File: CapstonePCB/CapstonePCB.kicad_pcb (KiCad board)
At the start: 2 copper layers, 4 parts, among them J1 Conn_02x40_Counter_Clockwise, J2 Barrel_Jack, U1 NUCLEO64-F411RE, U2 LP-MSPM0G3507

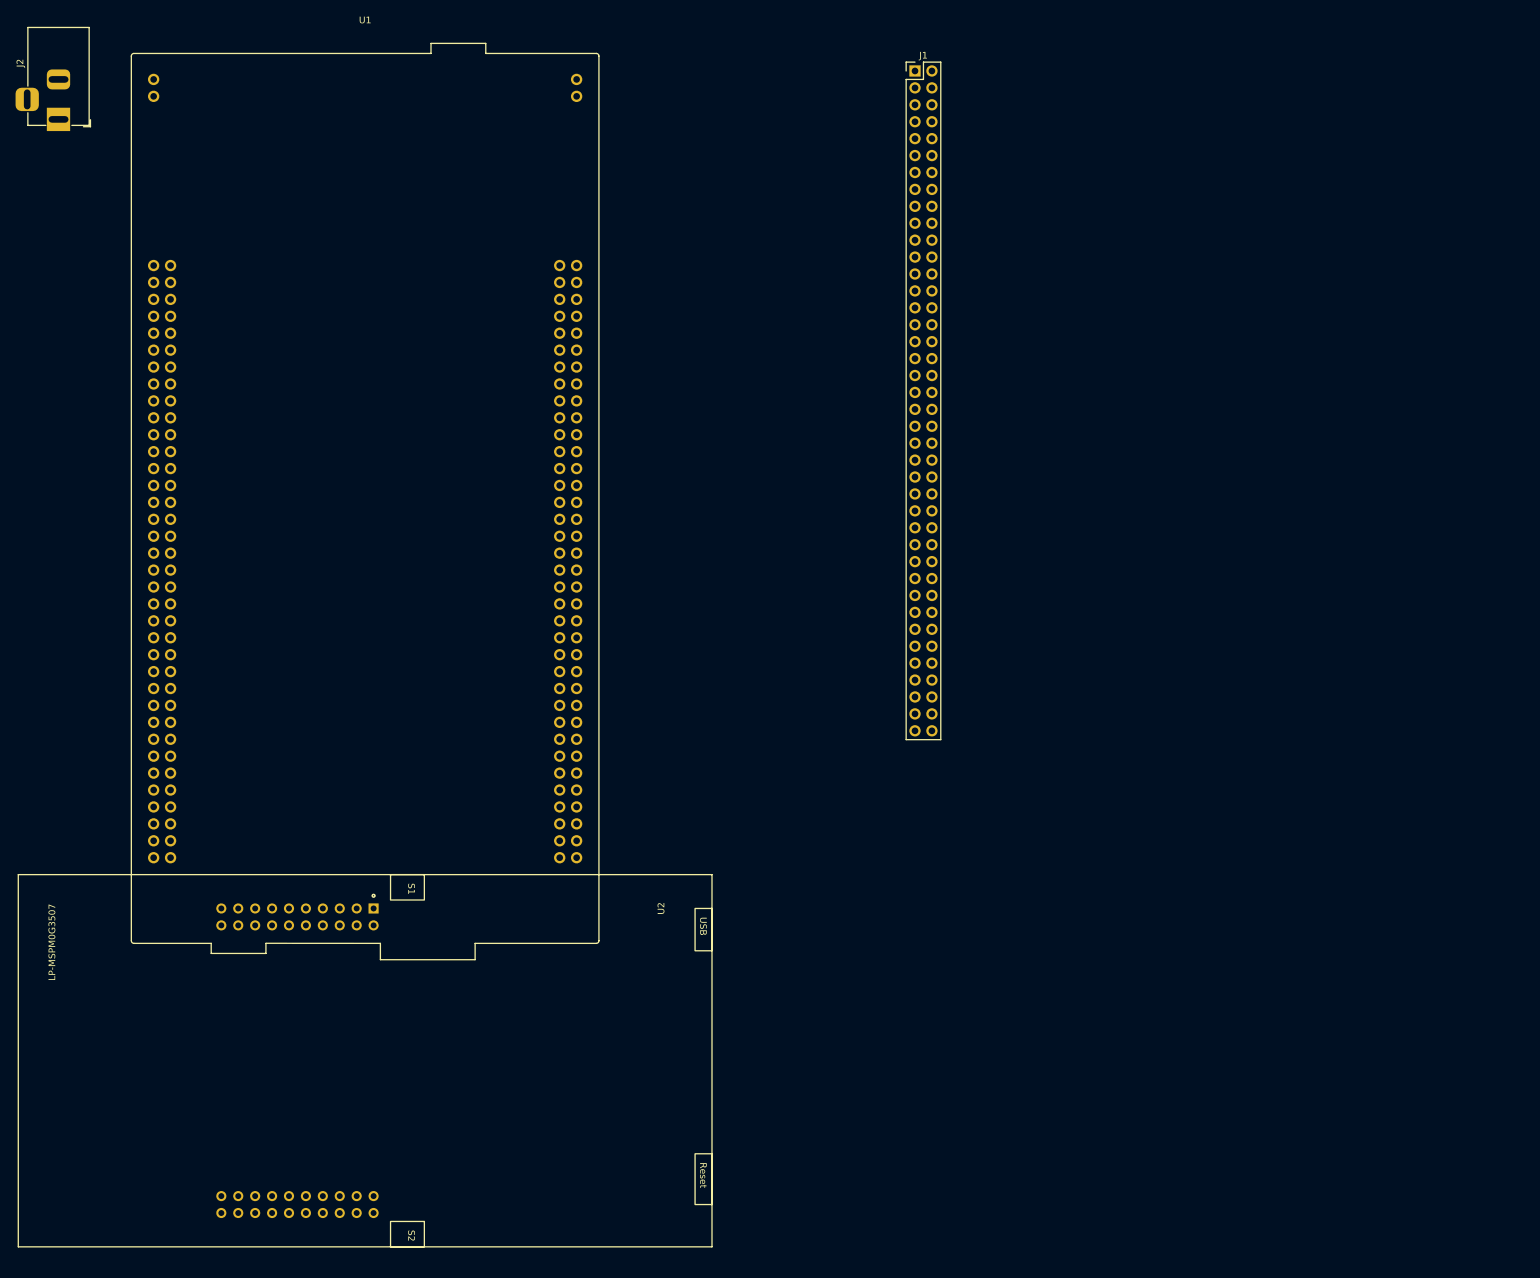
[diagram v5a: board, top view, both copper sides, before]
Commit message: Routed connections for header pins
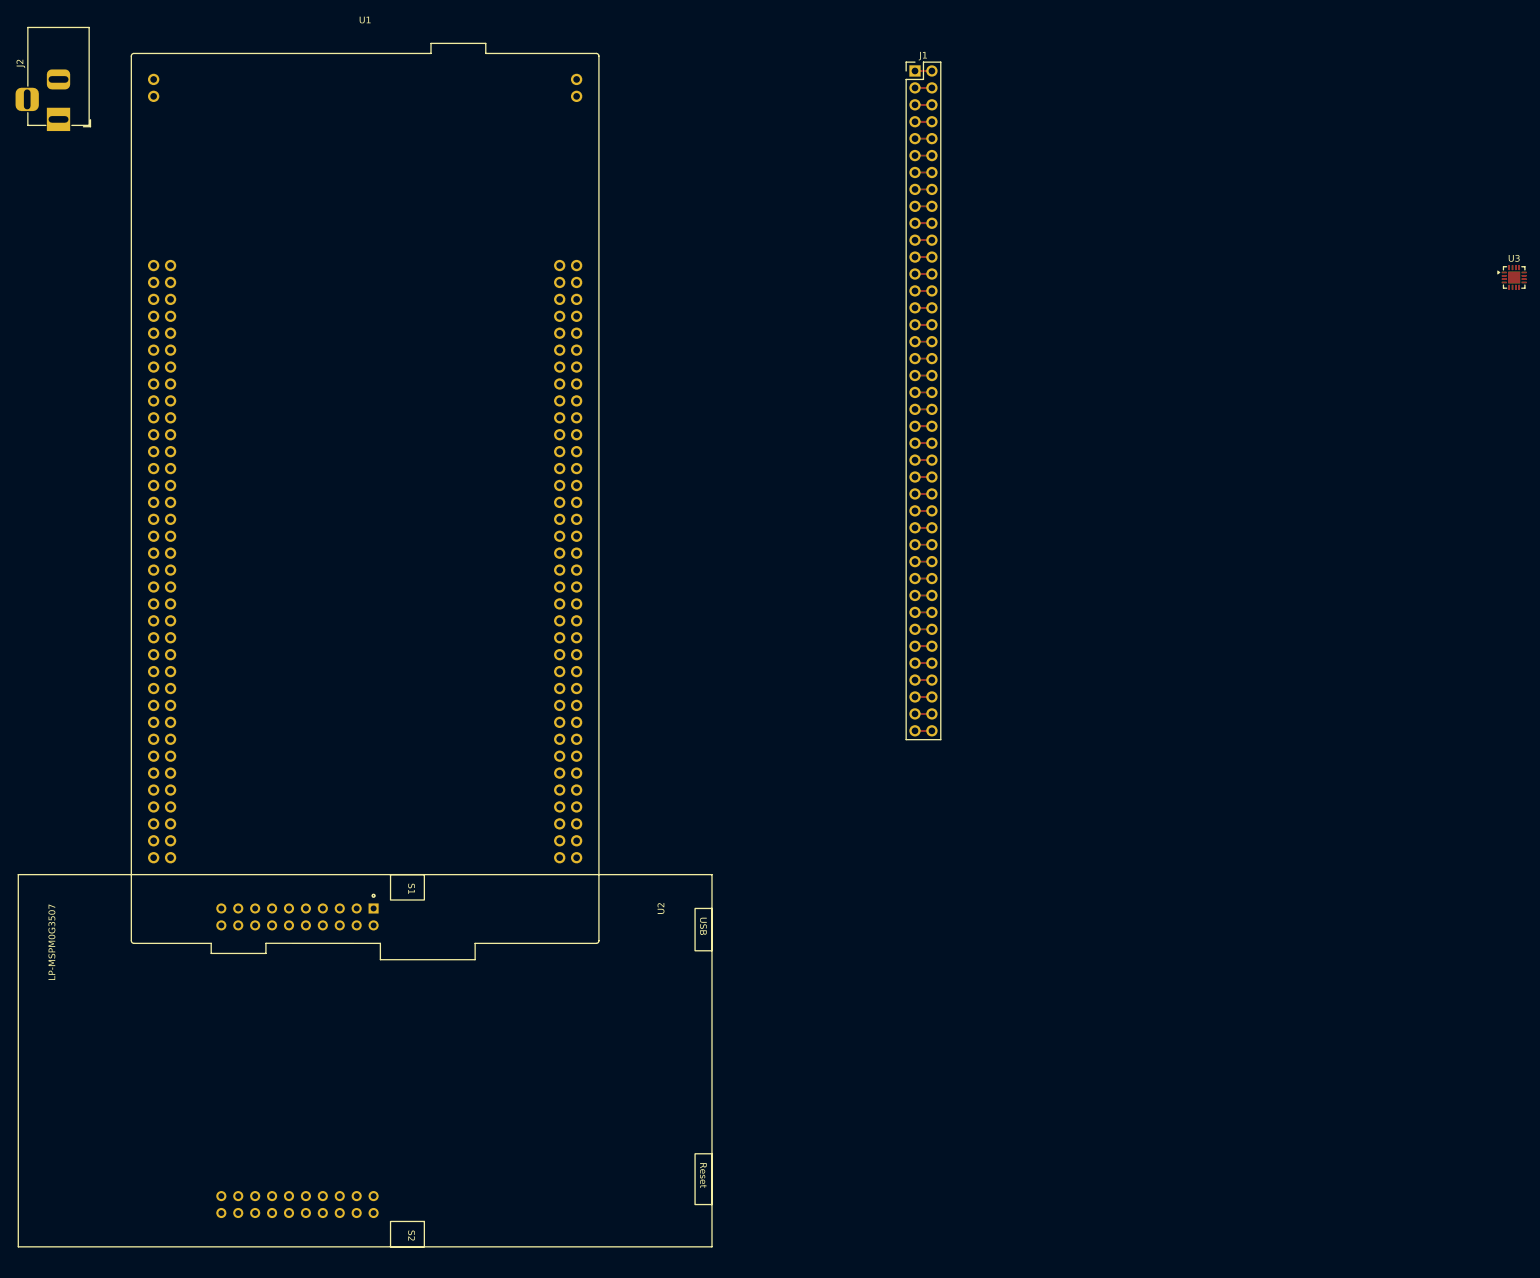
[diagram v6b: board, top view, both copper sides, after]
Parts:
- added U3: STSPIN220, Package_DFN_QFN:VQFN-16-1EP_3x3mm_P0.5mm_EP1.8x1.8mm, F.Cu at (237.3, 47.5)
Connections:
- J1 pad 10: unconnected-(J1-Pin_10-Pad10) -> Net-(J1-Pin_10)
- J1 pad 11: unconnected-(J1-Pin_11-Pad11) -> Net-(J1-Pin_11)
- J1 pad 12: unconnected-(J1-Pin_12-Pad12) -> Net-(J1-Pin_11)
- J1 pad 13: unconnected-(J1-Pin_13-Pad13) -> Net-(J1-Pin_13)
- J1 pad 14: unconnected-(J1-Pin_14-Pad14) -> Net-(J1-Pin_13)
- J1 pad 15: unconnected-(J1-Pin_15-Pad15) -> Net-(J1-Pin_15)
- J1 pad 16: unconnected-(J1-Pin_16-Pad16) -> Net-(J1-Pin_15)
- J1 pad 17: unconnected-(J1-Pin_17-Pad17) -> Net-(J1-Pin_17)
- J1 pad 18: unconnected-(J1-Pin_18-Pad18) -> Net-(J1-Pin_17)
- J1 pad 19: unconnected-(J1-Pin_19-Pad19) -> Net-(J1-Pin_19)
- J1 pad 2: Net-(J1-Pin_2) -> Net-(J1-Pin_1)
- J1 pad 20: unconnected-(J1-Pin_20-Pad20) -> Net-(J1-Pin_19)
- J1 pad 21: unconnected-(J1-Pin_21-Pad21) -> Net-(J1-Pin_21)
- J1 pad 22: unconnected-(J1-Pin_22-Pad22) -> Net-(J1-Pin_21)
- J1 pad 23: unconnected-(J1-Pin_23-Pad23) -> Net-(J1-Pin_23)
- J1 pad 24: unconnected-(J1-Pin_24-Pad24) -> Net-(J1-Pin_23)
- J1 pad 25: unconnected-(J1-Pin_25-Pad25) -> Net-(J1-Pin_25)
- J1 pad 26: unconnected-(J1-Pin_26-Pad26) -> Net-(J1-Pin_25)
- J1 pad 27: unconnected-(J1-Pin_27-Pad27) -> Net-(J1-Pin_27)
- J1 pad 28: unconnected-(J1-Pin_28-Pad28) -> Net-(J1-Pin_27)
- J1 pad 29: unconnected-(J1-Pin_29-Pad29) -> Net-(J1-Pin_29)
- J1 pad 30: unconnected-(J1-Pin_30-Pad30) -> Net-(J1-Pin_29)
- J1 pad 31: unconnected-(J1-Pin_31-Pad31) -> Net-(J1-Pin_31)
- J1 pad 32: unconnected-(J1-Pin_32-Pad32) -> Net-(J1-Pin_31)
- J1 pad 33: unconnected-(J1-Pin_33-Pad33) -> Net-(J1-Pin_33)
- J1 pad 34: unconnected-(J1-Pin_34-Pad34) -> Net-(J1-Pin_33)
- J1 pad 35: unconnected-(J1-Pin_35-Pad35) -> Net-(J1-Pin_35)
- J1 pad 36: unconnected-(J1-Pin_36-Pad36) -> Net-(J1-Pin_35)
- J1 pad 37: unconnected-(J1-Pin_37-Pad37) -> Net-(J1-Pin_37)
- J1 pad 38: unconnected-(J1-Pin_38-Pad38) -> Net-(J1-Pin_37)
- J1 pad 39: unconnected-(J1-Pin_39-Pad39) -> Net-(J1-Pin_39)
- J1 pad 4: unconnected-(J1-Pin_4-Pad4) -> Net-(J1-Pin_3)
- J1 pad 40: unconnected-(J1-Pin_40-Pad40) -> Net-(J1-Pin_39)
- J1 pad 41: unconnected-(J1-Pin_41-Pad41) -> Net-(J1-Pin_41)
- J1 pad 42: unconnected-(J1-Pin_42-Pad42) -> Net-(J1-Pin_41)
- J1 pad 43: unconnected-(J1-Pin_43-Pad43) -> Net-(J1-Pin_43)
- J1 pad 44: unconnected-(J1-Pin_44-Pad44) -> Net-(J1-Pin_43)
- J1 pad 45: unconnected-(J1-Pin_45-Pad45) -> Net-(J1-Pin_45)
- J1 pad 46: unconnected-(J1-Pin_46-Pad46) -> Net-(J1-Pin_45)
- J1 pad 47: unconnected-(J1-Pin_47-Pad47) -> Net-(J1-Pin_47)
- J1 pad 48: unconnected-(J1-Pin_48-Pad48) -> Net-(J1-Pin_47)
- J1 pad 49: unconnected-(J1-Pin_49-Pad49) -> Net-(J1-Pin_49)
- J1 pad 5: unconnected-(J1-Pin_5-Pad5) -> Net-(J1-Pin_5)
- J1 pad 50: unconnected-(J1-Pin_50-Pad50) -> Net-(J1-Pin_49)
- J1 pad 51: unconnected-(J1-Pin_51-Pad51) -> Net-(J1-Pin_51)
- J1 pad 52: unconnected-(J1-Pin_52-Pad52) -> Net-(J1-Pin_51)
- J1 pad 53: unconnected-(J1-Pin_53-Pad53) -> Net-(J1-Pin_53)
- J1 pad 54: unconnected-(J1-Pin_54-Pad54) -> Net-(J1-Pin_53)
- J1 pad 55: unconnected-(J1-Pin_55-Pad55) -> Net-(J1-Pin_55)
- J1 pad 56: unconnected-(J1-Pin_56-Pad56) -> Net-(J1-Pin_55)
- J1 pad 57: unconnected-(J1-Pin_57-Pad57) -> Net-(J1-Pin_57)
- J1 pad 58: unconnected-(J1-Pin_58-Pad58) -> Net-(J1-Pin_57)
- J1 pad 59: unconnected-(J1-Pin_59-Pad59) -> Net-(J1-Pin_59)
- J1 pad 6: unconnected-(J1-Pin_6-Pad6) -> Net-(J1-Pin_5)
- J1 pad 60: unconnected-(J1-Pin_60-Pad60) -> Net-(J1-Pin_59)
- J1 pad 61: unconnected-(J1-Pin_61-Pad61) -> Net-(J1-Pin_61)
- J1 pad 62: unconnected-(J1-Pin_62-Pad62) -> Net-(J1-Pin_61)
- J1 pad 63: unconnected-(J1-Pin_63-Pad63) -> Net-(J1-Pin_63)
- J1 pad 64: unconnected-(J1-Pin_64-Pad64) -> Net-(J1-Pin_63)
- J1 pad 65: unconnected-(J1-Pin_65-Pad65) -> Net-(J1-Pin_65)
- J1 pad 66: unconnected-(J1-Pin_66-Pad66) -> Net-(J1-Pin_65)
- J1 pad 67: unconnected-(J1-Pin_67-Pad67) -> Net-(J1-Pin_67)
- J1 pad 68: unconnected-(J1-Pin_68-Pad68) -> Net-(J1-Pin_67)
- J1 pad 69: unconnected-(J1-Pin_69-Pad69) -> Net-(J1-Pin_69)
- J1 pad 7: unconnected-(J1-Pin_7-Pad7) -> Net-(J1-Pin_7)
- J1 pad 70: unconnected-(J1-Pin_70-Pad70) -> Net-(J1-Pin_69)
- J1 pad 71: unconnected-(J1-Pin_71-Pad71) -> Net-(J1-Pin_71)
- J1 pad 72: unconnected-(J1-Pin_72-Pad72) -> Net-(J1-Pin_71)
- J1 pad 73: unconnected-(J1-Pin_73-Pad73) -> Net-(J1-Pin_73)
- J1 pad 74: unconnected-(J1-Pin_74-Pad74) -> Net-(J1-Pin_73)
- J1 pad 75: unconnected-(J1-Pin_75-Pad75) -> Net-(J1-Pin_75)
- J1 pad 76: unconnected-(J1-Pin_76-Pad76) -> Net-(J1-Pin_75)
- J1 pad 77: unconnected-(J1-Pin_77-Pad77) -> Net-(J1-Pin_77)
- J1 pad 78: Net-(J1-Pin_3) -> Net-(J1-Pin_77)
- J1 pad 79: Net-(J1-Pin_2) -> Net-(J1-Pin_79)
- J1 pad 8: unconnected-(J1-Pin_8-Pad8) -> Net-(J1-Pin_7)
- J1 pad 80: Net-(J1-Pin_1) -> Net-(J1-Pin_79)
- J1 pad 9: unconnected-(J1-Pin_9-Pad9) -> Net-(J1-Pin_10)
- U1 pad 8: unconnected-(U1-GND-Pad8) -> GNDREF
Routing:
- net Net-(J1-Pin_79): track 0.00 -> 2.54 mm
- net Net-(J1-Pin_77): track 0.00 -> 2.54 mm
- net Net-(J1-Pin_75): track 0.00 -> 2.54 mm
- net Net-(J1-Pin_73): track 0.00 -> 2.54 mm
- net Net-(J1-Pin_71): track 0.00 -> 2.54 mm
- net Net-(J1-Pin_7): track 0.00 -> 2.54 mm
- net Net-(J1-Pin_69): track 0.00 -> 2.54 mm
- net Net-(J1-Pin_67): track 0.00 -> 2.54 mm
- net Net-(J1-Pin_65): track 0.00 -> 2.54 mm
- net Net-(J1-Pin_63): track 0.00 -> 2.54 mm
- net Net-(J1-Pin_61): track 0.00 -> 2.54 mm
- net Net-(J1-Pin_59): track 0.00 -> 2.54 mm
- net Net-(J1-Pin_57): track 0.00 -> 2.54 mm
- net Net-(J1-Pin_55): track 0.00 -> 2.54 mm
- net Net-(J1-Pin_53): track 0.00 -> 2.54 mm
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
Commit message: Added by-pass capacitors
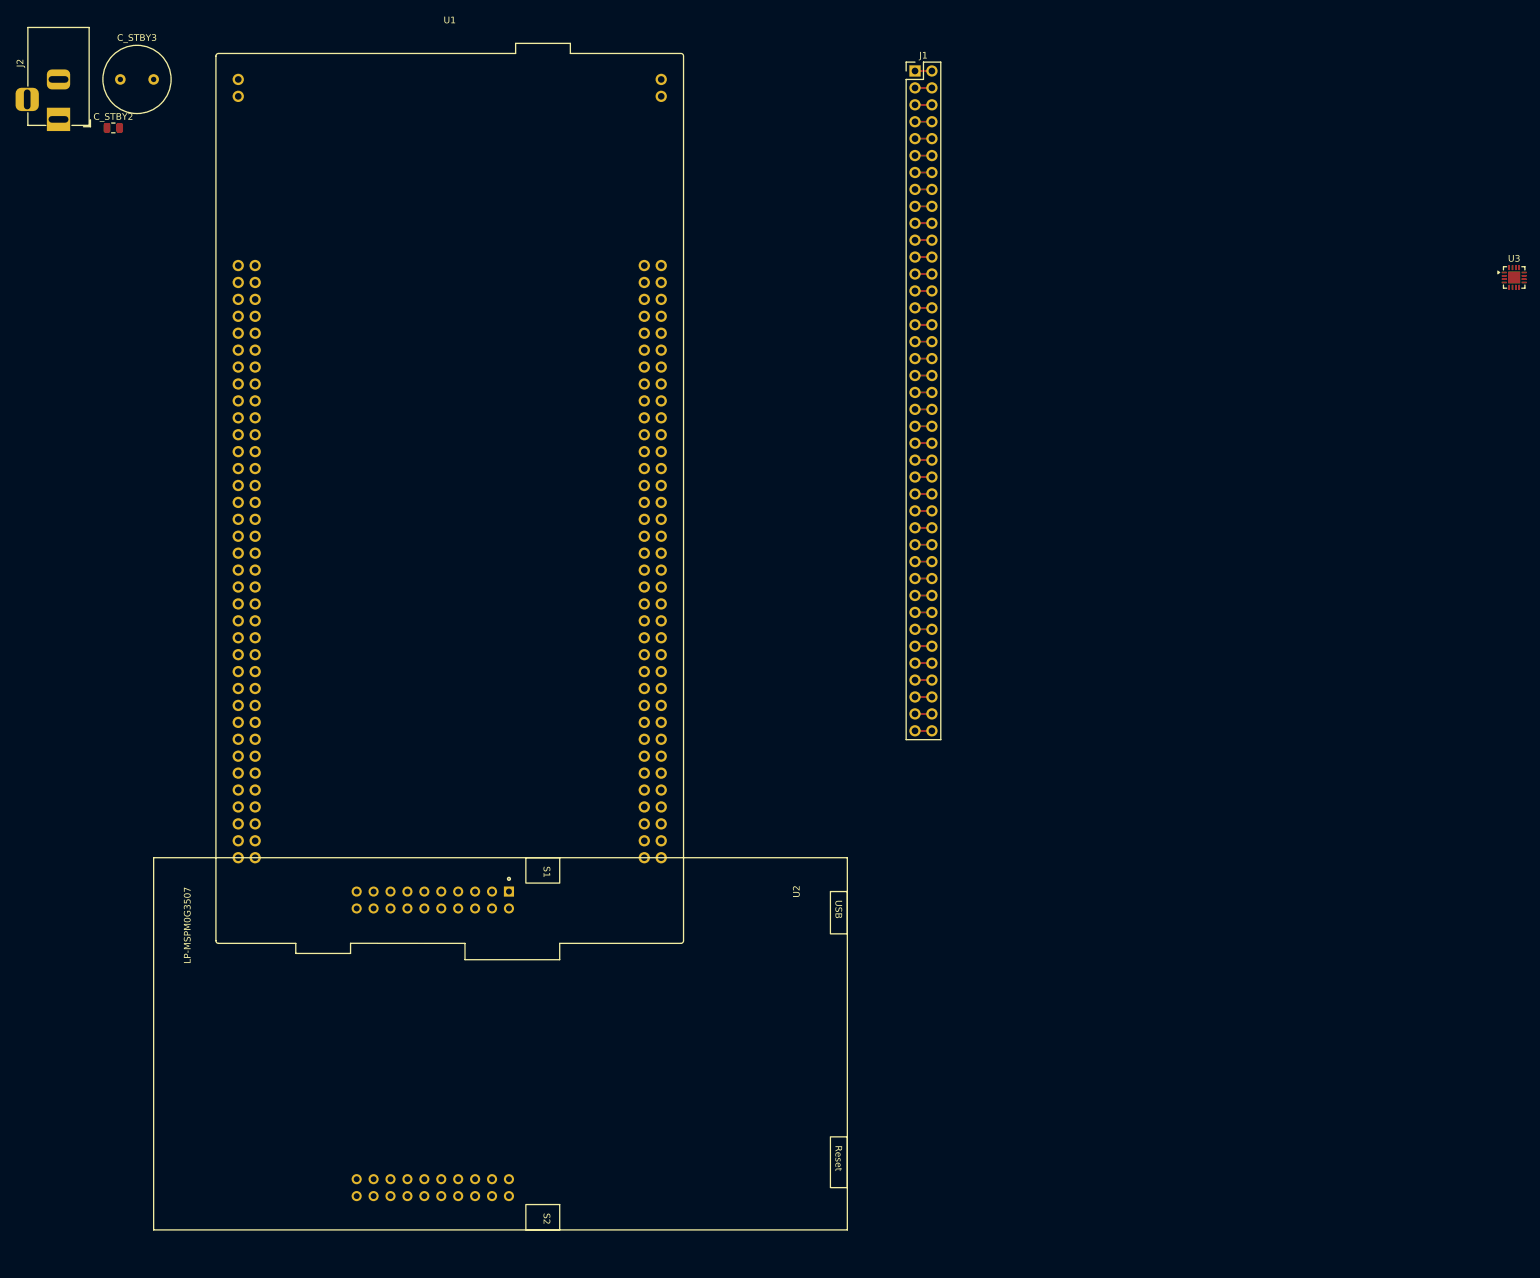
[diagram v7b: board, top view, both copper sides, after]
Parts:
- added C_STBY2: 0.1 uf, Capacitor_SMD:C_0805_2012Metric, F.Cu at (27.0, 25.1)
- added C_STBY3: 47 uf, Capacitor_THT:C_Radial_D10.0mm_H20.0mm_P5.00mm, F.Cu at (28.0, 17.8)
- moved U2 20.5 mm to (83.8, 162.6)
- moved U1 12.7 mm to (45.7, 45.7)
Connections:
- J2 pad 1: unconnected-(J2-Pad1) -> +12V

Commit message: Added LDOs for 5v and 3.3v rails
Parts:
- added U5: LM7805_TO220, Package_TO_SOT_THT:TO-220-3_Vertical, F.Cu at (17.8, 33.0)
- added U6: TLV1117-33, Package_TO_SOT_SMD:SOT-223-3_TabPin2, F.Cu at (19.7, 43.2)
